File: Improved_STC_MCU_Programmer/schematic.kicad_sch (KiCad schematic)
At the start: 18 parts, among them J1 USB B socket, J2 Target board, Q1 AO3400A, SW1 RESET, SW2 Target supply voltage, U1 CH340N, U2 AMS1117-3.3

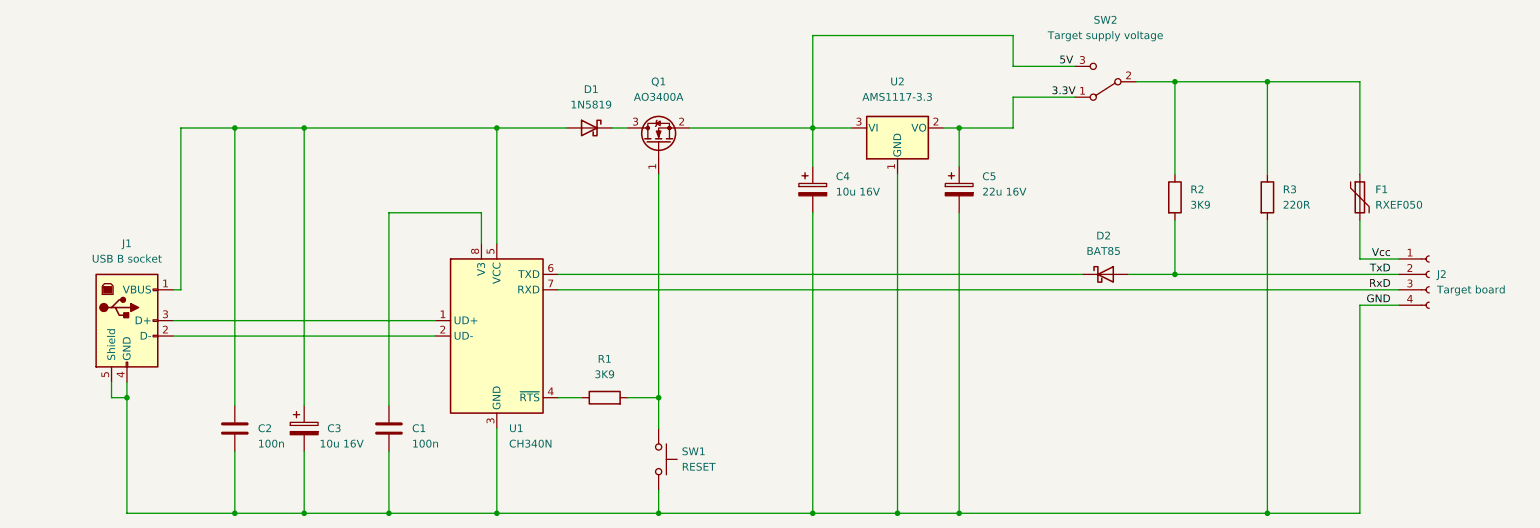
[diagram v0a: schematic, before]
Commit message: Fixed power cycle issue with improved programmer
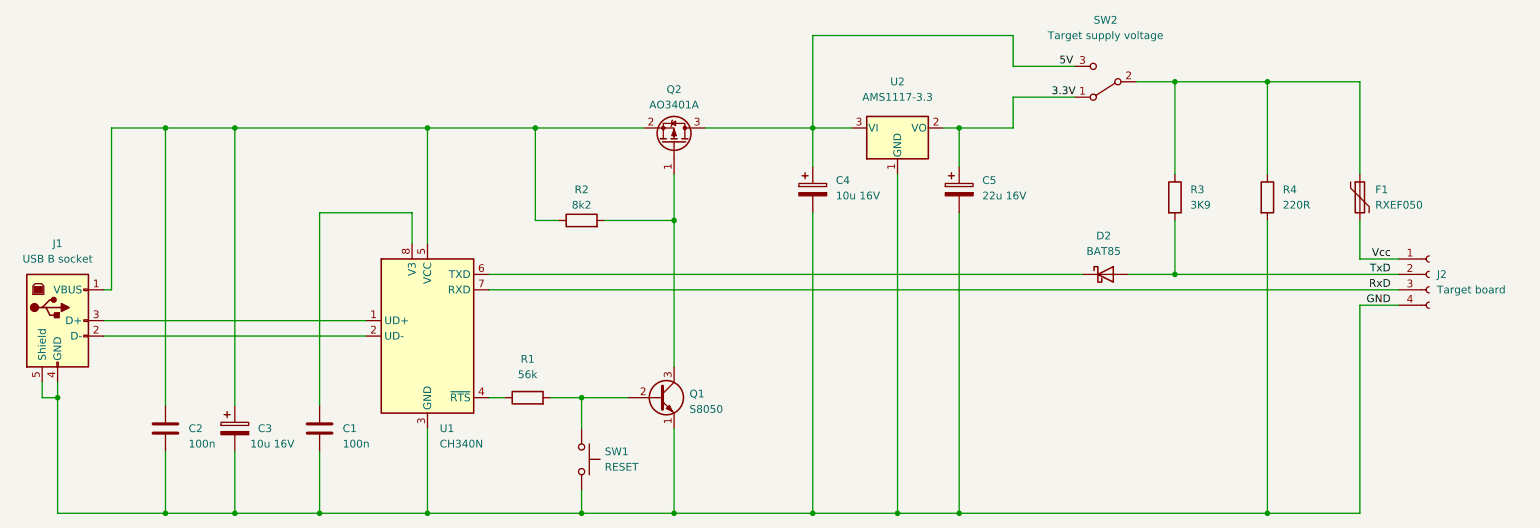
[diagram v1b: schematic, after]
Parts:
- removed D1: 1N5819, Diode_THT:D_DO-41_SOD81_P10.16mm_Horizontal, symbol Diode:1N5819
- removed Q1: AO3400A, Package_TO_SOT_SMD:SOT-23, symbol Transistor_FET:AO3400A
- added Q1: S8050, Package_TO_SOT_THT:TO-92_Inline, symbol Transistor_BJT:S8050
- added Q2: AO3401A, Package_TO_SOT_SMD:SOT-23, symbol Transistor_FET:AO3401A
- added R2: 8k2, symbol Device:R
- R1: value 3K9 -> 56k
- renumbered R2 to R3, R3 to R4
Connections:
- net 5V: now also Q2.3 (D)
- net GND: now also Q1.1 (E)
- net at R1.2, SW1.1: now also Q1.2 (B)
- net at C2.1, C3.1, J1.1 (VBUS)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: now also Q2.2 (S), R2.1
- new net: Q1.3 (C), Q2.1 (G), R2.2
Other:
- moved on the sheet: C1, C2, C3, J1, R1, SW1, U1

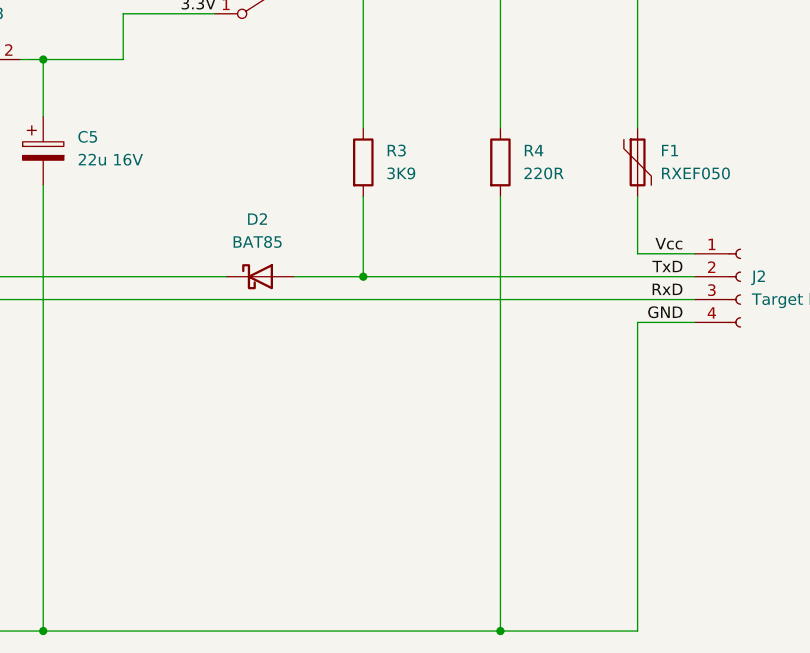
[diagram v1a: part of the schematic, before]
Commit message: Added power indicator to improved programmer
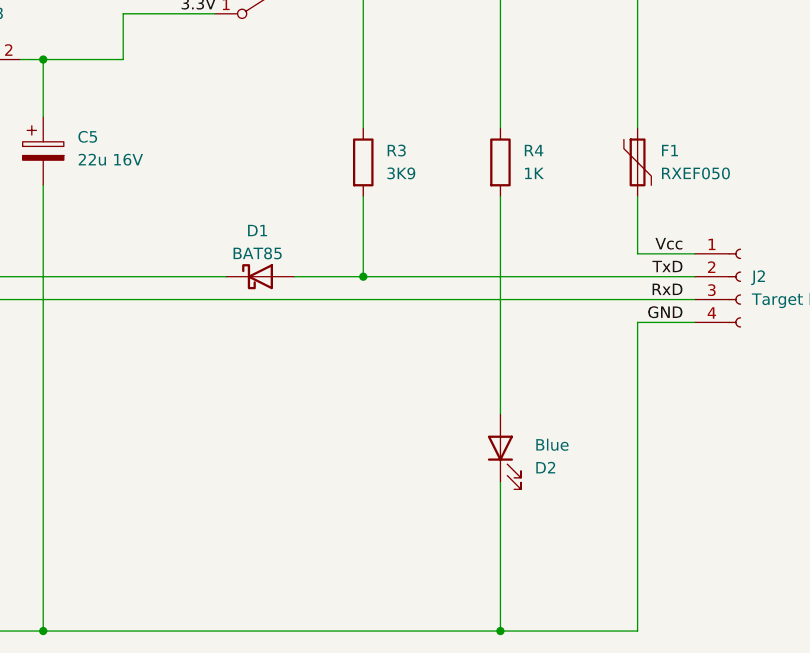
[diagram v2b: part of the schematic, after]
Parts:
- added D2: Blue, symbol Device:LED
- R4: value 220R -> 1K
- renumbered D2 to D1
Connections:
- net GND: now also D2.1 (K); no longer R4.2
- new net: D2.2 (A), R4.2
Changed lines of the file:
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@@
     (title "Improved STC MCU programmer")
     (date "2023-05-01")
-    (rev "1.1")
+    (rev "1.2")
     (company "(c) 2022 Vincent DEFERT. Licensed under the CC BY 4.0 license.")
     (comment 1 "For use with STCGAL-patched in automatic mode (-A rts and -a options).")
@@
   (junction (at 120.65 130.81) (diameter 0) (color 0 0 0 0)
   )
+  (junction (at 233.68 130.81) (diameter 0) (color 0 0 0 0)
+  )
   (junction (at 182.88 130.81) (diameter 0) (color 0 0 0 0)
   )
@@
   (junction (at 63.5 67.31) (diameter 0) (color 0 0 0 0)
   )
-  (junction (at 233.68 130.81) (diameter 0) (color 0 0 0 0)
-  )
   (junction (at 95.25 67.31) (diameter 0) (color 0 0 0 0)
   )
@@
     (stroke (width 0) (type default))
   )
+  (wire (pts (xy 182.88 130.81) (xy 233.68 130.81))
+    (stroke (width 0) (type default))
+  )
+  (wire (pts (xy 95.25 67.31) (xy 113.03 67.31))
+    (stroke (width 0) (type default))
+  )
+  (wire (pts (xy 41.91 101.6) (xy 85.09 101.6))
+    (stroke (width 0) (type default))
+  )
+  (wire (pts (xy 140.97 67.31) (xy 158.75 67.31))
+    (stroke (width 0) (type default))
+  )
   (wire (pts (xy 233.68 130.81) (xy 248.92 130.81))
     (stroke (width 0) (type default))
   )
-  (wire (pts (xy 95.25 67.31) (xy 113.03 67.31))
-    (stroke (width 0) (type default))
-  )
-  (wire (pts (xy 41.91 101.6) (xy 85.09 101.6))
-    (stroke (width 0) (type default))
-  )
-  (wire (pts (xy 140.97 67.31) (xy 158.75 67.31))
-    (stroke (width 0) (type default))
-  )
   (wire (pts (xy 105.41 91.44) (xy 203.2 91.44))
     (stroke (width 0) (type default))
@@
     (stroke (width 0) (type default))
   )
-  (wire (pts (xy 182.88 130.81) (xy 233.68 130.81))
-    (stroke (width 0) (type default))
-  )
   (wire (pts (xy 218.44 59.69) (xy 218.44 74.93))
     (stroke (width 0) (type default))
@@
     (stroke (width 0) (type default))
   )
+  (wire (pts (xy 233.68 114.3) (xy 233.68 130.81))
+    (stroke (width 0) (type default))
+  )
   (wire (pts (xy 158.75 67.31) (xy 158.75 73.66))
     (stroke (width 0) (type default))
@@
     (stroke (width 0) (type default))
   )
-  (wire (pts (xy 233.68 82.55) (xy 233.68 130.81))
-    (stroke (width 0) (type default))
-  )
   (wire (pts (xy 233.68 59.69) (xy 233.68 74.93))
     (stroke (width 0) (type default))
@@
   )
   (wire (pts (xy 135.89 82.55) (xy 135.89 106.68))
+    (stroke (width 0) (type default))
+  )
+  (wire (pts (xy 233.68 82.55) (xy 233.68 106.68))
     (stroke (width 0) (type default))
   )
@@
       (effects (font (size 1.27 1.27)) (justify left))
     )
-    (property "Value" "220R" (at 236.22 80.0099 0)
+    (property "Value" "1K" (at 236.22 80.0099 0)
       (effects (font (size 1.27 1.27)) (justify left))
     )
@@
   (symbol (lib_id "Diode:BAT85") (at 207.01 91.44 0) (unit 1)
     (in_bom yes) (on_board yes) (dnp no) (fields_autoplaced)
-    (property "Reference" "D2" (at 206.6925 85.09 0)
-      (effects (font (size 1.27 1.27)))
-    )
-    (property "Value" "BAT85" (at 206.6925 87.63 0)
+    (property "Reference" "D1" (at 206.6925 86.36 0)
+      (effects (font (size 1.27 1.27)))
+    )
+    (property "Value" "BAT85" (at 206.6925 88.9 0)
       (effects (font (size 1.27 1.27)))
     )
@@
       (effects (font (size 1.27 1.27)) hide)
     )
+    (pin "1")
+    (pin "2")
+    (instances
+      (project "schematic"
+        (path "/5b91eaaa-a6f9-4814-bd74-db0e5fb19bcf"
+          (reference "D1") (unit 1)
+        )
+      )
+    )
+  )
+  (symbol (lib_id "Device:LED") (at 233.68 110.49 90) (unit 1)
+    (in_bom yes) (on_board yes) (dnp no)
+    (property "Reference" "D2" (at 237.49 112.7125 90)
+      (effects (font (size 1.27 1.27)) (justify right))
+    )
+    (property "Value" "Blue" (at 237.49 110.1725 90)
+      (effects (font (size 1.27 1.27)) (justify right))
+    )
+    (property "Footprint" "" (at 233.68 110.49 0)
+      (effects (font (size 1.27 1.27)) hide)
+    )
+    (property "Datasheet" "~" (at 233.68 110.49 0)
+      (effects (font (size 1.27 1.27)) hide)
+    )

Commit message: Replaced blue LED with a red one (lower Vf)
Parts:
- D2: value Blue -> Red
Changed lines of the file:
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@@
       (effects (font (size 1.27 1.27)) (justify right))
     )
-    (property "Value" "Blue" (at 237.49 110.1725 90)
+    (property "Value" "Red" (at 237.49 110.1725 90)
       (effects (font (size 1.27 1.27)) (justify right))
     )

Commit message: Changed pull-up resistor value
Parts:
- removed D1: BAT85, Diode_THT:D_DO-35_SOD27_P7.62mm_Horizontal, symbol Diode:BAT85
- added D1: 1N5819, Diode_THT:D_DO-41_SOD81_P10.16mm_Horizontal, symbol Diode:1N5819
- R3: value 3K9 -> 1K8
- renumbered R4 to R5
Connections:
- net TxD: now also D1.2 (A)
- net at U1.6 (TXD): now also D1.1 (K)
